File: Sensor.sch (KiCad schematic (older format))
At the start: 5 parts, among them U34 ICM-42688-P

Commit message: PVT
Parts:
- renumbered C131 to C126, C132 to C127, C133 to C128, L12 to L8, U34 to U32
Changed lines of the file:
@@
 encoding utf-8
 Sheet 16 24
-Title "Phoenix DVT"
-Date "2020-05-18"
+Title "Phoenix PVT"
+Date "2020-07-19"
 Rev "1"
 Comp ""
@@
 AR Path="/5E44687D" Ref="U?"  Part="1"
 AR Path="/5E44623C/5E44687D" Ref="U?"  Part="1"
-AR Path="/5E4EB435/5E44687D" Ref="U34"  Part="1"
-F 0 "U34" H 6000 4650 50  0000 C CNN
+AR Path="/5E4EB435/5E44687D" Ref="U32"  Part="1"
+F 0 "U32" H 6000 4650 50  0000 C CNN
 F 1 "ICM-42688-P" H 6000 3350 50  0000 C CNN
 F 2 "Phoenix:LGA14_3.0x2.5_P0.5" H 6000 4000 50  0001 C CNN
@@
 SDO
 $Comp
-L supply-alias:GND #PWR0291
+L supply-alias:GND #PWR0279
 U 1 1 5F569604
 P 4300 3900
-F 0 "#PWR0291" H 4300 3650 50  0001 C CNN
+F 0 "#PWR0279" H 4300 3650 50  0001 C CNN
 F 1 "GND" H 4300 3750 50  0000 C CNN
 F 2 "" H 4300 3900 50  0001 C CNN
@@
 NoConn ~ 5100 4400
 $Comp
-L passive:C C133
+L passive:C C128
 U 1 1 5F56B475
 P 4700 3700
-F 0 "C133" H 4800 3750 50  0000 L CNN
+F 0 "C128" H 4800 3750 50  0000 L CNN
 F 1 "100n" H 4800 3650 50  0000 L CNN
 F 2 "Capacitor-Chip:C_CHIP_1005_Hand_NoSilk" H 4800 3600 50  0001 C CNN
@@
 Connection ~ 4700 3900
 $Comp
-L passive:C C131
+L passive:C C126
 U 1 1 5F56C446
 P 4300 3700
-F 0 "C131" H 4400 3750 50  0000 L CNN
+F 0 "C126" H 4400 3750 50  0000 L CNN
 F 1 "10u" H 4400 3650 50  0000 L CNN
 F 2 "Capacitor-Chip:C_CHIP_1005_Hand_NoSilk" H 4400 3600 50  0001 C CNN
@@
 AR Path="/5E65EBEC/5F57AD1E" Ref="L?"  Part="1"
 AR Path="/5E4A98E7/5F57AD1E" Ref="L?"  Part="1"
-AR Path="/5E4EB435/5F57AD1E" Ref="L12"  Part="1"
-F 0 "L12" V 4235 3500 50  0000 C CNN
+AR Path="/5E4EB435/5F57AD1E" Ref="L8"  Part="1"
+F 0 "L8" V 4235 3500 50  0000 C CNN
 F 1 "600" V 4144 3500 50  0000 C CNN
 F 2 "Inductor-Chip:L_CHIP_1005_Hand_NoSilk" H 4100 3400 50  0001 C CNN
@@
 Connection ~ 4300 3500
 $Comp
-L passive:C C132
+L passive:C C127
 U 1 1 5F588122
 P 4700 3100
-F 0 "C132" H 4800 3150 50  0000 L CNN
+F 0 "C127" H 4800 3150 50  0000 L CNN
 F 1 "100n" H 4800 3050 50  0000 L CNN
 F 2 "Capacitor-Chip:C_CHIP_1005_Hand_NoSilk" H 4800 3000 50  0001 C CNN
@@
 	4700 3900 5100 3900
 $Comp
-L supply-alias:GND #PWR0293
+L supply-alias:GND #PWR0281
 U 1 1 5F58E423
 P 4700 3200
-F 0 "#PWR0293" H 4700 2950 50  0001 C CNN
+F 0 "#PWR0281" H 4700 2950 50  0001 C CNN
 F 1 "GND" H 4700 3050 50  0000 C CNN
 F 2 "" H 4700 3200 50  0001 C CNN
@@
 	6900 4500 9900 4500
 $Comp
-L supply-value:+3V3 #PWR0292
+L supply-value:+3V3 #PWR0280
 U 1 1 5EFDBC2F
 P 4700 2900
-F 0 "#PWR0292" H 4700 2750 50  0001 C CNN
+F 0 "#PWR0280" H 4700 2750 50  0001 C CNN
 F 1 "+3V3" H 4700 3040 50  0000 C CNN
 F 2 "" H 4700 2900 50  0001 C CNN
@@
 Connection ~ 4700 2900
 $Comp
-L supply-value:+3V3 #PWR0290
+L supply-value:+3V3 #PWR0278
 U 1 1 5EFDC1BF
 P 3700 3500
-F 0 "#PWR0290" H 3700 3350 50  0001 C CNN
+F 0 "#PWR0278" H 3700 3350 50  0001 C CNN
 F 1 "+3V3" H 3700 3640 50  0000 C CNN
 F 2 "" H 3700 3500 50  0001 C CNN
@@
 NoConn ~ 5100 4500
 $Comp
-L supply-alias:GND #PWR0294
+L supply-alias:GND #PWR0282
 U 1 1 5F56A9C4
 P 4900 4300
-F 0 "#PWR0294" H 4900 4050 50  0001 C CNN
+F 0 "#PWR0282" H 4900 4050 50  0001 C CNN
 F 1 "GND" H 4900 4150 50  0000 C CNN
 F 2 "" H 4900 4300 50  0001 C CNN

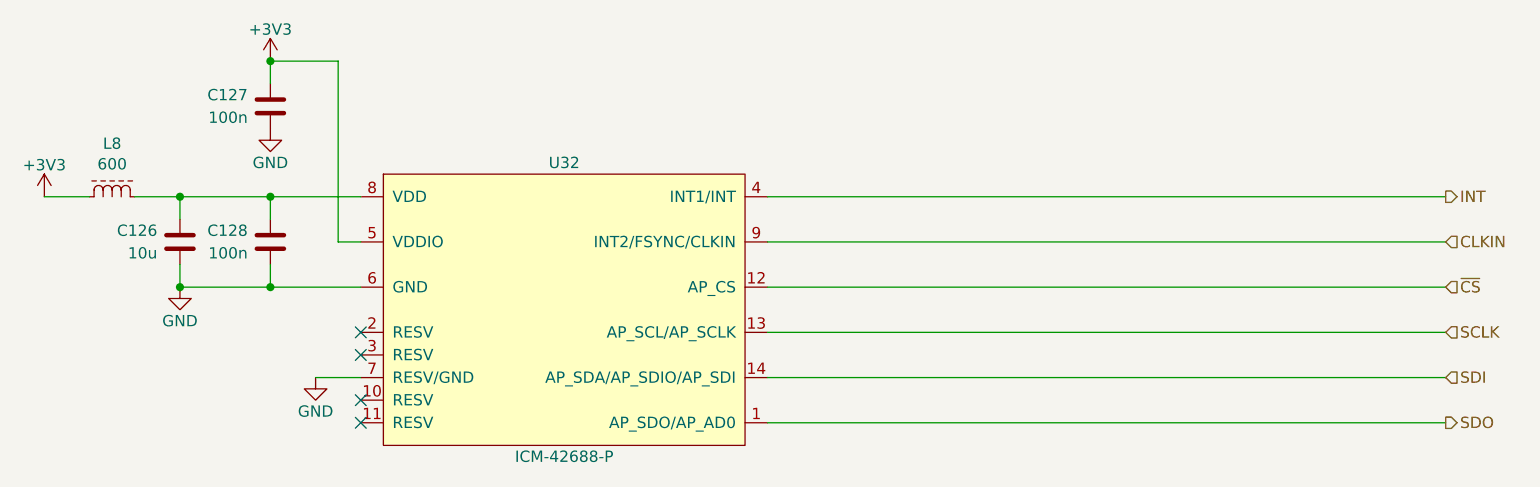
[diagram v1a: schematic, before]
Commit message: SBUにTVSダイオードを追加
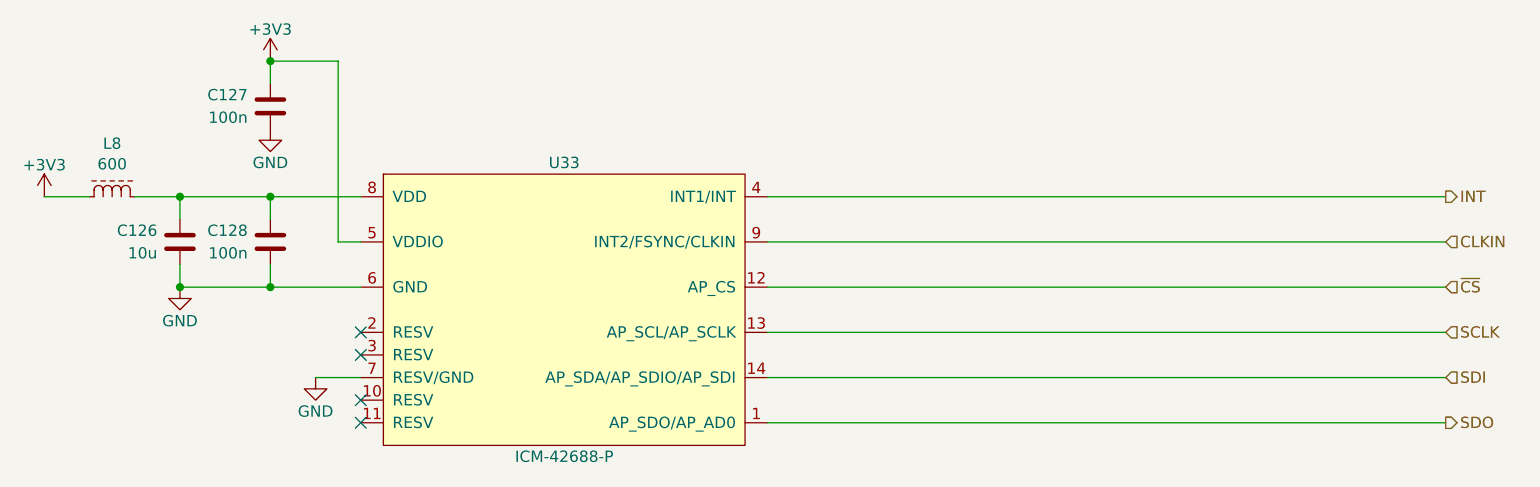
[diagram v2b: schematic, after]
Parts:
- renumbered U32 to U33
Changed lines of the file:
@@
 AR Path="/5E44687D" Ref="U?"  Part="1"
 AR Path="/5E44623C/5E44687D" Ref="U?"  Part="1"
-AR Path="/5E4EB435/5E44687D" Ref="U32"  Part="1"
-F 0 "U32" H 6000 4650 50  0000 C CNN
+AR Path="/5E4EB435/5E44687D" Ref="U33"  Part="1"
+F 0 "U33" H 6000 4650 50  0000 C CNN
 F 1 "ICM-42688-P" H 6000 3350 50  0000 C CNN
 F 2 "Phoenix:LGA14_3.0x2.5_P0.5" H 6000 4000 50  0001 C CNN
